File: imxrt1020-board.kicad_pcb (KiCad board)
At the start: 2 copper layers, 102.9 x 68.6 mm, 200 parts, among them J1 Micro_SD_Card_Det, J10 CASTELATED, J11 CASTELATED, J12 CASTELATED, J13 CASTELATED, J14 CASTELATED, J15 CASTELATED, J16 CASTELATED, J17 CASTELATED, J18 CASTELATED, J19 CASTELATED, J2 USB_OTG, J20 CASTELATED, J21 CASTELATED, J22 CASTELATED, J23 CASTELATED, J24 CASTELATED, J25 CASTELATED, J26 CASTELATED, J27 CASTELATED, J28 CASTELATED, J29 CASTELATED, J3 Conn_02x20_Odd_Even, J30 CASTELATED, J31 CASTELATED, J32 CASTELATED, J33 CASTELATED, J34 CASTELATED, J35 CASTELATED, J36 CASTELATED, J37 CASTELATED, J38 CASTELATED, J39 CASTELATED, J4 CASTELATED, J40 CASTELATED, J41 CASTELATED, J42 CASTELATED, J43 CASTELATED, J44 GS2, J45 GS2, J46 PWR_IN, J47 JTAG, J48 Conn_01x06, J49 CASTELATED, J5 CASTELATED, J50 CASTELATED, J51 CASTELATED, J52 CASTELATED, J53 CASTELATED, J54 CASTELATED, J55 CASTELATED, J56 CASTELATED, J57 CASTELATED, J58 SI-50196-F, J59 CASTELATED, J6 CASTELATED, J60 CASTELATED, J61 CASTELATED, J62 CASTELATED, J63 CASTELATED, J64 CASTELATED, J65 CASTELATED, J66 CASTELATED, J67 CASTELATED, J68 CASTELATED, J69 CASTELATED, J7 CASTELATED, J70 CASTELATED, J71 CASTELATED, J72 CASTELATED, J73 CASTELATED, J74 CASTELATED, J75 CASTELATED, J76 CASTELATED, J77 CASTELATED, J78 CASTELATED, J79 CASTELATED, J8 CASTELATED, J80 CASTELATED, J81 Conn_01x07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

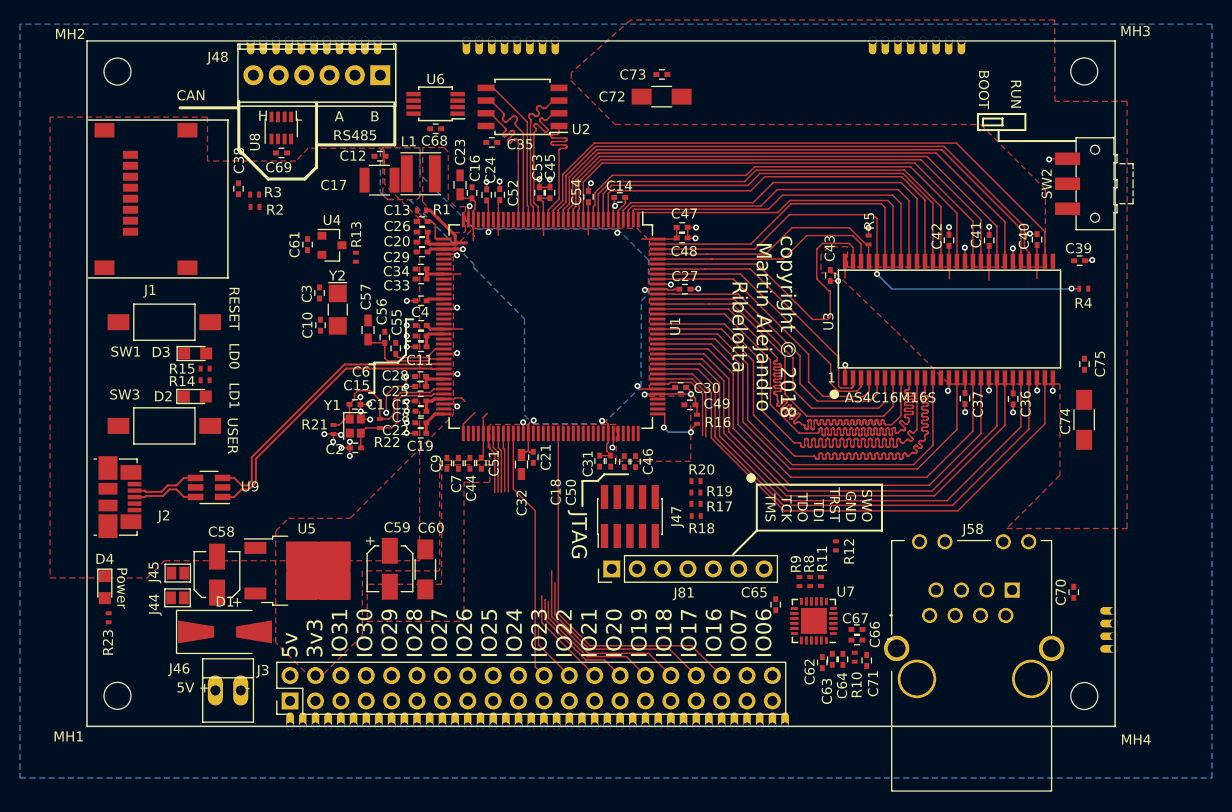
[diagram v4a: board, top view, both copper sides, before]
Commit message: Finished major route on 6/6mils tech.
Signed-off-by: Martin Ribelotta <martinribelotta@gmail.com>
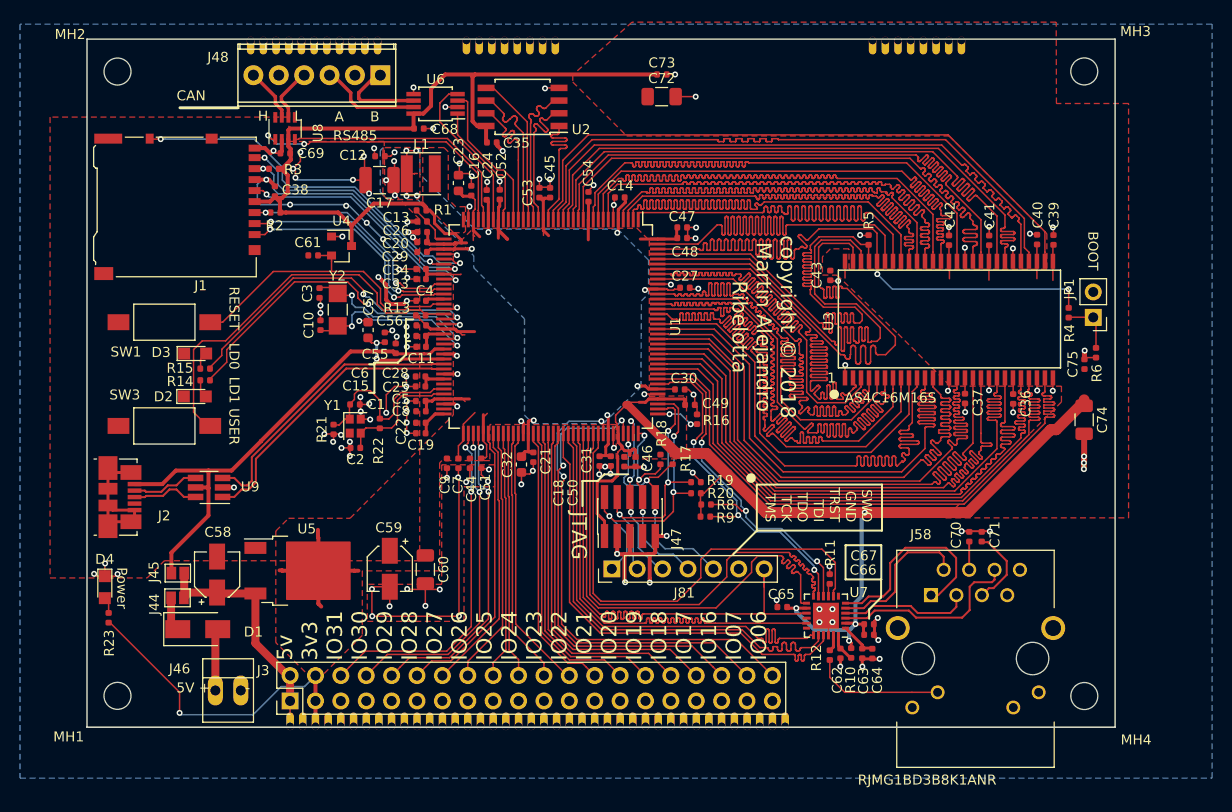
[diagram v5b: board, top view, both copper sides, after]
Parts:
- removed J59, J60, J61, J62: CASTELATED, local:castelated_pad
- removed SW2: BOOT0, Buttons_Switches_SMD:SW_SPDT_CK-JS102011SAQN
- added JP1: ROMBOOT, Connector_PinHeader_2.54mm:PinHeader_1x02_P2.54mm_Vertical, F.Cu at (208.5, 98.9)
- added R6: 1K, Resistor_SMD:R_0402_1005Metric, F.Cu at (208.7, 102.4)
- C1, C10, C11, C12, C13, C14, C15, C16, C18, C19, C2, C20, C21, C22, C24, C25, C26, C27, C28, C29, C3, C30, C31, C33, C34, C35, C36, C37, C38, C39, C4, C40, C41, C42, C43, C44, C45, C46, C47, C48, C49, C5, C50, C51, C52, C53, C54, C55, C56, C6, C61, C62, C63, C64, C65, C66, C67, C68, C69, C7, C70, C71, C73, C75, C8, C9: footprint Capacitors_SMD:C_0402 -> Capacitor_SMD:C_0402_1005Metric
- C17: footprint Capacitors_SMD:C_1210 -> Capacitor_SMD:C_1210_3225Metric
- C23, C32, C57: footprint Capacitors_SMD:C_0603_HandSoldering -> Capacitor_SMD:C_0603_1608Metric
- C58, C59: footprint Capacitors_SMD:CP_Elec_4x4.5 -> Capacitor_SMD:CP_Elec_4x4.5
- C60, C72, C74: footprint Capacitors_SMD:C_1206_HandSoldering -> Capacitor_SMD:C_1206_3216Metric
- D1: value 1N4001 -> S1GTR; footprint Diodes_SMD:D_SMA-SMB_Universal_Handsoldering -> Diode_SMD:D_SMA
- J1: footprint Connectors_Card:MicroSd_Wurth_693072010801 -> Connector_Card:microSD_HC_Hirose_DM3AT-SF-PEJM5
- J58: value SI-50196-F -> RJMG1BD3B8K1ANR; footprint Connectors:RJ45_TRANSFO -> local:CONN_RJMG1BD3B8K1ANR
- L1: footprint Inductors_SMD:L_Taiyo-Yuden_MD-4040 -> Inductor_SMD:L_Taiyo-Yuden_MD-4040
- R1, R10, R11, R12, R13, R14, R15, R16, R17, R18, R19, R2, R20, R21, R22, R23, R3, R4, R5, R8, R9: footprint Resistors_SMD:R_0402_NoSilk -> Resistor_SMD:R_0402_1005Metric
- moved C71 16.9 mm to (197.3, 120.9), turned to 90 degrees
- moved R8 13.0 mm to (169.7, 117.6), turned to 0 degrees
- moved C70 11.8 mm to (196.0, 120.9)
- moved R9 11.4 mm to (169.6, 118.8), turned to 0 degrees
- moved R12 11.0 mm to (182.1, 132.7), turned to 270 degrees
- moved R13 8.71 mm to (141.2, 98.7), turned to 180 degrees
- moved J58 7.77 mm to (196.7, 133.0)
- moved R18 6.70 mm to (165.2, 113.1), turned to 270 degrees
- moved R17 5.03 mm to (166.4, 113.1), turned to 270 degrees
- moved C38 3.65 mm to (126.6, 86.3)
- moved C39 3.33 mm to (204.5, 91.2), turned to 90 degrees
- moved J1 3.24 mm to (116.8, 87.8)
- moved R3 3.22 mm to (126.5, 84.0), turned to 180 degrees
- moved C63 3.06 mm to (185.3, 132.5)
- moved C64 2.99 mm to (186.3, 132.5)
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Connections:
- J2 pad 4: (no net) -> Net-(J2-Pad4)
- J47 pad 7: (no net) -> Net-(J47-Pad7)
- J58 pad 1: /GPIO/ENET_TX+ -> GND
- J58 pad 2: Net-(C70-Pad1) -> GND
- MH1 pad 1: (no net) -> Net-(MH1-Pad1)
- MH2 pad 1: (no net) -> Net-(MH2-Pad1)
- MH3 pad 1: (no net) -> Net-(MH3-Pad1)
- MH4 pad 1: (no net) -> Net-(MH4-Pad1)
- R12 pad 2: Net-(J58-PadYA) -> /GPIO/ENET_LED
- U1 pad 128: (no net) -> /MEMORY/SEM_DQS
- U1 pad 27: (no net) -> /MEMORY/GPIO3_24
- U1 pad 41: (no net) -> /MEMORY/SD_SW
- U1 pad 66: (no net) -> Net-(U1-Pad66)
- U1 pad 71: (no net) -> Net-(U1-Pad71)
- U3 pad 40: (no net) -> Net-(U3-Pad40)
- U7 pad 16: (no net) -> Net-(U7-Pad16)
- U7 pad 18: (no net) -> Net-(U7-Pad18)
- U7 pad 7: (no net) -> Net-(U7-Pad7)
- U8 pad 5: (no net) -> Net-(U8-Pad5)
- U8 pad 8: (no net) -> Net-(U8-Pad8)
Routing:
- net +3V3: track 67.9 -> 342.6 mm, vias 0 -> 5
- net GND: track 69.0 -> 232.5 mm, vias 57 -> 135
- net /GPIO/ENET_CRS_DV: track 0.00 -> 54.3 mm
- net /GPIO/UART1_RX: track 0.00 -> 48.9 mm, vias 0 -> 2
- net /GPIO/UART1_TX: track 0.00 -> 48.5 mm, vias 0 -> 2
- net /GPIO/ENET_TXD0: track 0.00 -> 48.1 mm
- net /GPIO/ENET_RXD0: track 0.00 -> 48.1 mm
- net /GPIO/ENET_RXD1: track 0.00 -> 48.0 mm
- net /GPIO/ENET_RX_ER: track 0.00 -> 48.0 mm
- net /GPIO/ENET_TX_EN: track 0.00 -> 48.0 mm
- net /GPIO/ENET_TXD1: track 0.00 -> 48.0 mm
- net /GPIO/ENET_TX_CLK: track 0.00 -> 48.0 mm
- net /POWER/PWR_IN1: track 5.41 -> 49.9 mm
- net /MEMORY/SDRAM_A1: track 24.6 -> 64.3 mm
- net Net-(R13-Pad1): track 0.00 -> 39.4 mm
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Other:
- board size 102.9 x 68.6 mm -> 102.9 x 68.8 mm
- net class SDCK added: clearance 0.381, trace_width 0.1524, via_dia 0.6, via_drill 0.3
- board text added: "BOOT"
- board text removed: "RUN BOOT"

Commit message: Update some footprints and retune SDRAM for broken nets
Signed-off-by: Martin Ribelotta <martinribelotta@gmail.com>
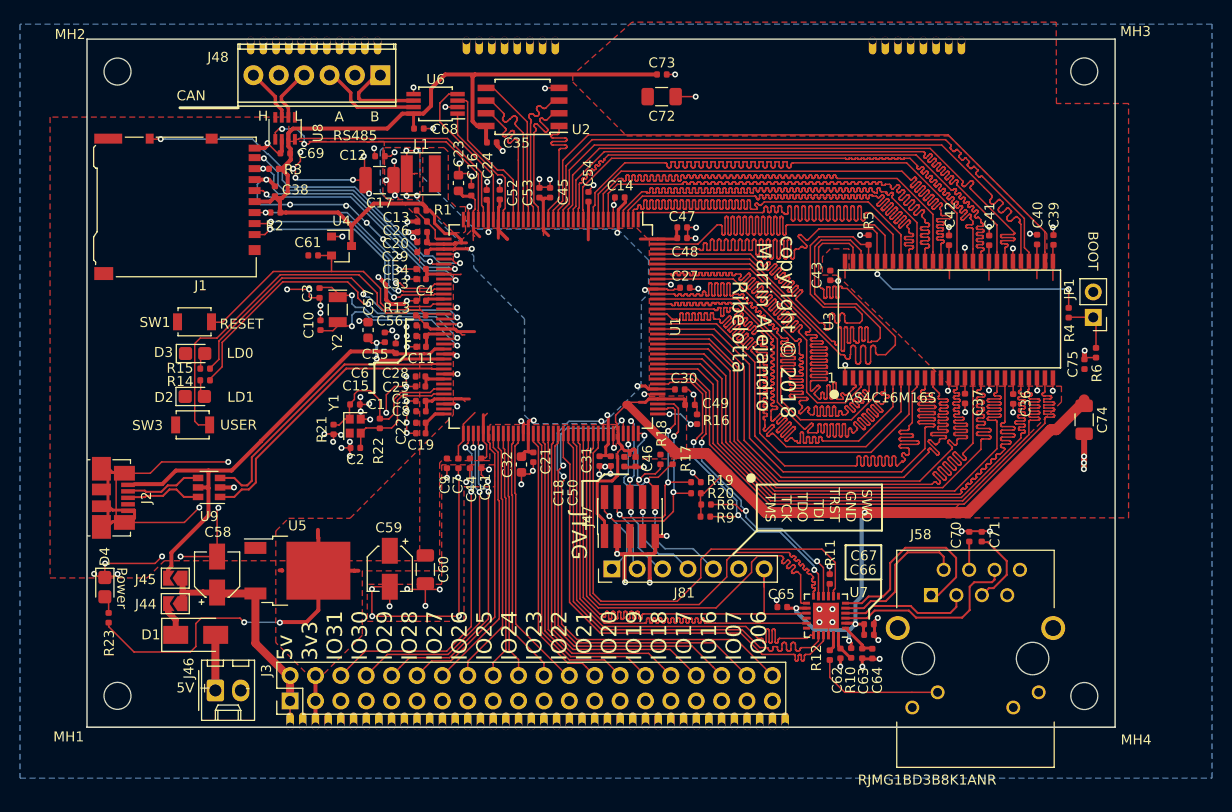
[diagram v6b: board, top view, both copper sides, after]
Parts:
- D2, D3, D4: footprint LEDs:LED_0805 -> LED_SMD:LED_0805_2012Metric_Castellated
- J2: footprint Connectors_USB:USB_Micro-B_Molex_47346-0001 -> Connector_USB:USB_Micro-B_Molex_47346-0001
- J44, J45: footprint Connectors:GS2 -> Jumper:SolderJumper-2_P1.3mm_Open_TrianglePad1.0x1.5mm
- J46: footprint Connectors:PINHEAD1-2 -> Connector_Molex:Molex_KK-254_AE-6410-02A_1x02_P2.54mm_Vertical
- J47: footprint Pin_Headers:Pin_Header_Straight_2x05_Pitch1.27mm_SMD -> Connector_PinHeader_1.27mm:PinHeader_2x05_P1.27mm_Vertical_SMD
- SW1, SW3: footprint Buttons_Switches_SMD:SW_SPST_FSMSM -> Button_Switch_SMD:SW_SPST_B3U-1000P
- U4: footprint TO_SOT_Packages_SMD:SOT-23 -> Package_TO_SOT_SMD:SOT-23
- U5: footprint TO_SOT_Packages_SMD:TO-252-2 -> Package_TO_SOT_SMD:TO-252-2
- U9: footprint TO_SOT_Packages_SMD:SOT-23-6_Handsoldering -> Package_TO_SOT_SMD:SOT-23-6
- Y1: footprint Crystals:Crystal_SMD_2016-4pin_2.0x1.6mm -> Crystal:Crystal_SMD_2016-4Pin_2.0x1.6mm
- Y2: footprint Crystals:Crystal_SMD_MicroCrystal_CC7V-T1A-2pin_3.2x1.5mm_HandSoldering -> Crystal:Crystal_SMD_MicroCrystal_CC7V-T1A-2Pin_3.2x1.5mm
- moved SW1 3.02 mm to (118.5, 99.4)
- moved SW3 2.83 mm to (118.3, 109.7)
- moved J44 0.62 mm to (116.6, 127.6), turned to 180 degrees
- moved D1 0.61 mm to (118.6, 130.7)
- moved J45 0.56 mm to (116.6, 125.0), turned to 180 degrees
- moved J2 0.55 mm to (110.4, 117.0)
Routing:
- net GND: track 232.5 -> 276.6 mm, vias 135 -> 142
- net +3V3: track 342.6 -> 338.3 mm, vias 5 -> 6
- net /MEMORY/SDRAM_A1: track 64.3 -> 62.6 mm
- net /MEMORY/SDRAM_UDQM: track 63.6 -> 62.6 mm
- net Net-(R14-Pad1): track 33.7 -> 34.4 mm
- net Net-(D1-Pad2): track 6.23 -> 5.57 mm
- net Net-(R15-Pad1): track 32.2 -> 32.9 mm
- net /POWER/PWR_IN1: track 49.9 -> 50.5 mm
- net Net-(R13-Pad1): track 39.4 -> 39.9 mm

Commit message: Update images
Signed-off-by: Martin Ribelotta <martinribelotta@gmail.com>
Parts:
- J48: footprint TerminalBlocks_Phoenix:TerminalBlock_Phoenix_MPT-2.54mm_6pol -> TerminalBlock_Phoenix:TerminalBlock_Phoenix_MPT-0,5-6-2.54_1x06_P2.54mm_Horizontal
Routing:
- net GND: track 276.6 -> 277.9 mm, vias 142 -> 143
